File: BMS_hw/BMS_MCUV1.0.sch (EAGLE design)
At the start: 1 part

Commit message: Revert "Merge branch 'hw' of https://github.com/kunal-GF/GF_BMS into hw"
This reverts commit cb819c5a256ea6b478828d222d8978a164d41654, reversing
changes made to 1a0582993ac0a8851db6f9d974378484a723c9b0.
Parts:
- removed MCU1: PIC32MK0512GPE064-I/PT, GreenFuel:PIC32MK0512GPE064-I/PT
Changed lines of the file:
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@@
 <setting verticaltext="up"/>
 </settings>
-<grid distance="0.1" unitdist="inch" unit="inch" style="lines" multiple="1" display="yes" altdistance="0.01" altunitdist="inch" altunit="inch"/>
+<grid distance="0.1" unitdist="inch" unit="inch" style="lines" multiple="1" display="no" altdistance="0.01" altunitdist="inch" altunit="inch"/>
 <layers>
 <layer number="1" name="Top" color="4" fill="1" visible="no" active="no"/>
@@
 <part name="FRAME1" library="frames" library_urn="urn:adsk.eagle:library:229" deviceset="A3L-LOC" device=""/>
 <part name="FRAME2" library="frames" library_urn="urn:adsk.eagle:library:229" deviceset="A3L-LOC" device=""/>
-<part name="MCU1" library="GreenFuel" deviceset="PIC32MK0512GPE064-I/PT" device=""/>
 </parts>
 <sheets>
@@
 <instances>
 <instance part="FRAME1" gate="G$1" x="0" y="0"/>
-<instance part="MCU1" gate="G$1" x="190.5" y="142.24"/>
 </instances>
 <busses>

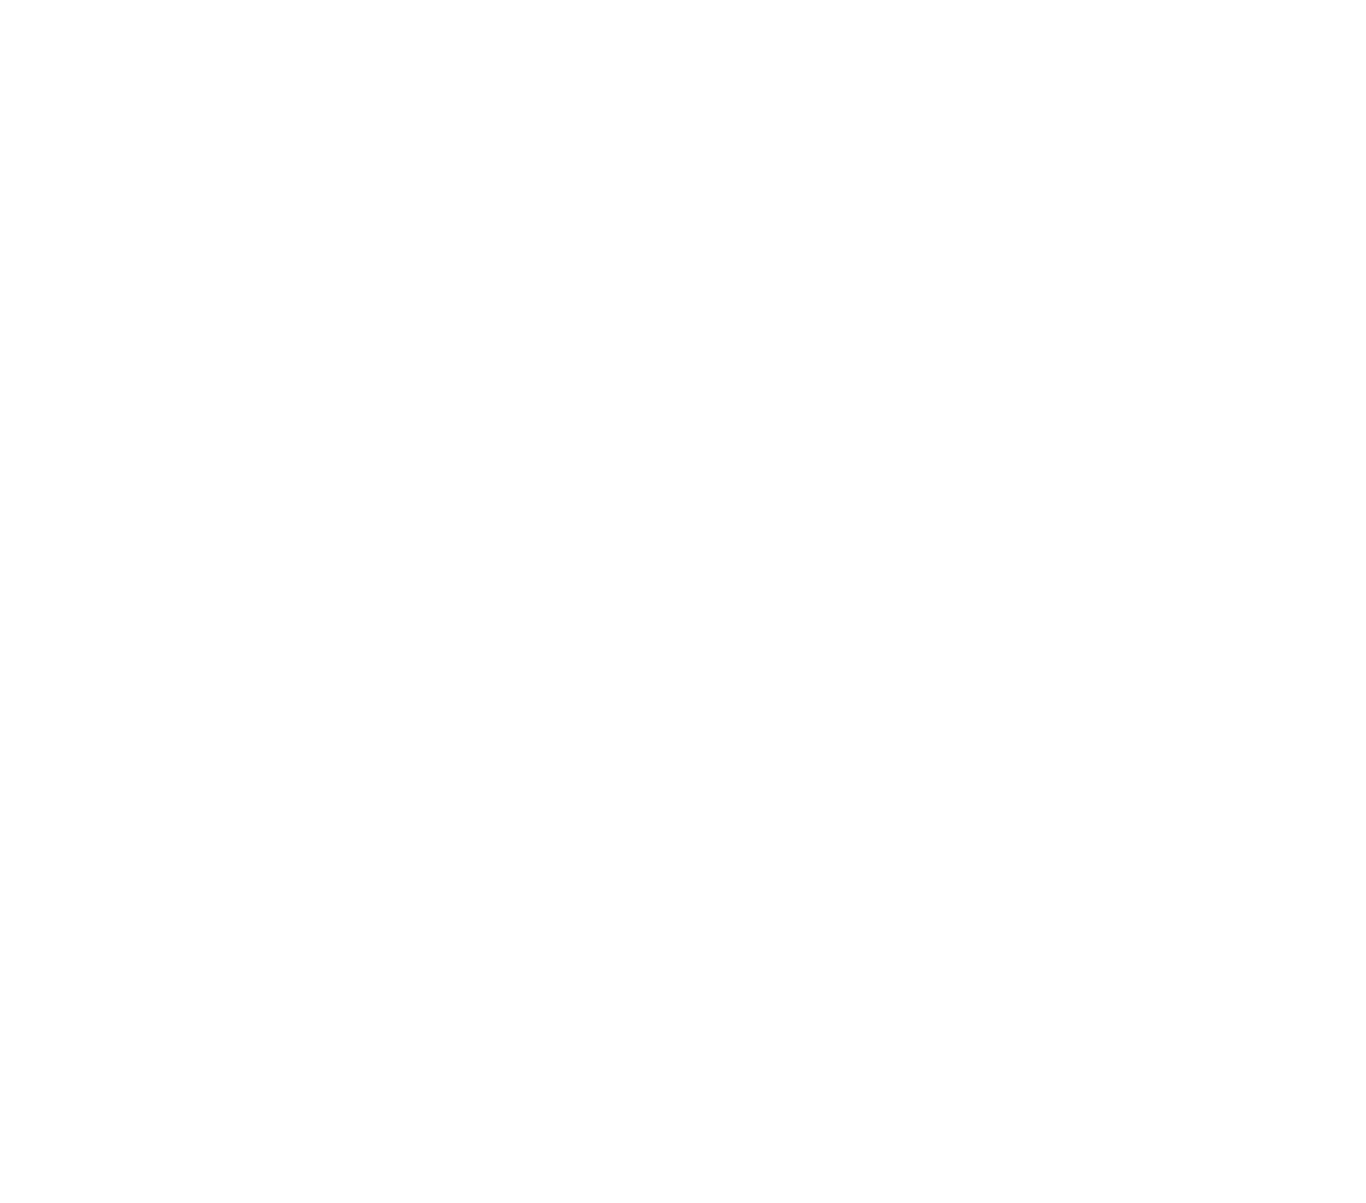
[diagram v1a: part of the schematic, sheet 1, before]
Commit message: update library ignore mcu
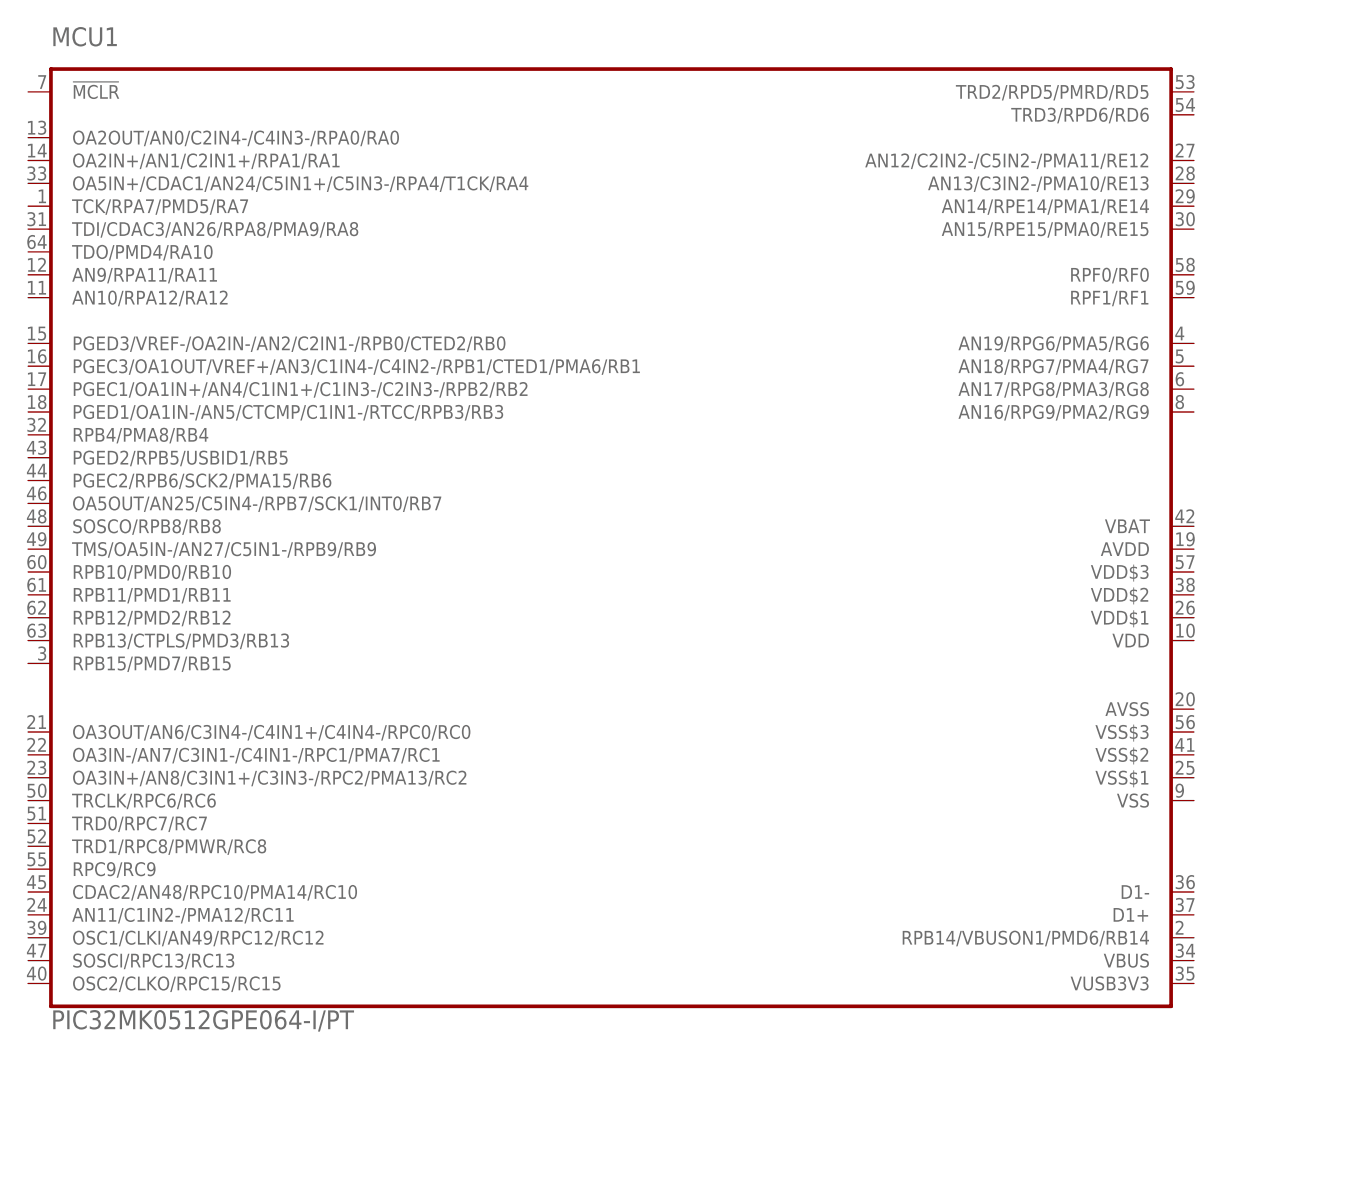
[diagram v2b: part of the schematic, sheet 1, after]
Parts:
- added MCU1: PIC32MK0512GPE064-I/PT, GreenFuel:PIC32MK0512GPE064-I/PT
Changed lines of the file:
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@@
 <setting verticaltext="up"/>
 </settings>
-<grid distance="0.1" unitdist="inch" unit="inch" style="lines" multiple="1" display="no" altdistance="0.01" altunitdist="inch" altunit="inch"/>
+<grid distance="0.1" unitdist="inch" unit="inch" style="lines" multiple="1" display="yes" altdistance="0.01" altunitdist="inch" altunit="inch"/>
 <layers>
 <layer number="1" name="Top" color="4" fill="1" visible="no" active="no"/>
@@
 <part name="FRAME1" library="frames" library_urn="urn:adsk.eagle:library:229" deviceset="A3L-LOC" device=""/>
 <part name="FRAME2" library="frames" library_urn="urn:adsk.eagle:library:229" deviceset="A3L-LOC" device=""/>
+<part name="MCU1" library="GreenFuel" deviceset="PIC32MK0512GPE064-I/PT" device=""/>
 </parts>
 <sheets>
@@
 <instances>
 <instance part="FRAME1" gate="G$1" x="0" y="0"/>
+<instance part="MCU1" gate="G$1" x="190.5" y="142.24"/>
 </instances>
 <busses>
